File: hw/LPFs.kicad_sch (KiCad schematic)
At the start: 26 parts, among them K201 G6K-2, K202 G6K-2, K203 G6K-2, Q201 2N7002H, Q202 2N7002H, Q203 2N7002H

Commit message: Timing now closes at 121MHz. But output still does not produce any signal on my scope. Shit.
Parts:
- removed C201, C211: 100nF X7R 50V, Capacitor_SMD:C_0603_1608Metric, symbol Device:C
- L201, L204: MPN CW252016-1R2J -> 1008LS-122XJR; Mouser Part Number 1008LS-222 -> (none)
- L202, L205: MFG muRata -> (none); MPN LQW2UASR56G00L -> 1008CS-561X; Mouser Part Number 0805CS-391XGLC -> (none); Mouser_PN 81-LQW2UASR56G00L -> (none)
- L203, L206: MFG Bourns -> (none); MPN CW252016-R27J -> 1008CS-271XGRC; Mouser Part Number 0805CS-271 XGLC -> (none); Mouser_PN 652-CW252016-R27J -> 994-1008CS-271XGRC
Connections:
- net RFin: now also K201.4, K202.4, K203.4
- net RFout: now also K201.5, K202.5, K203.5

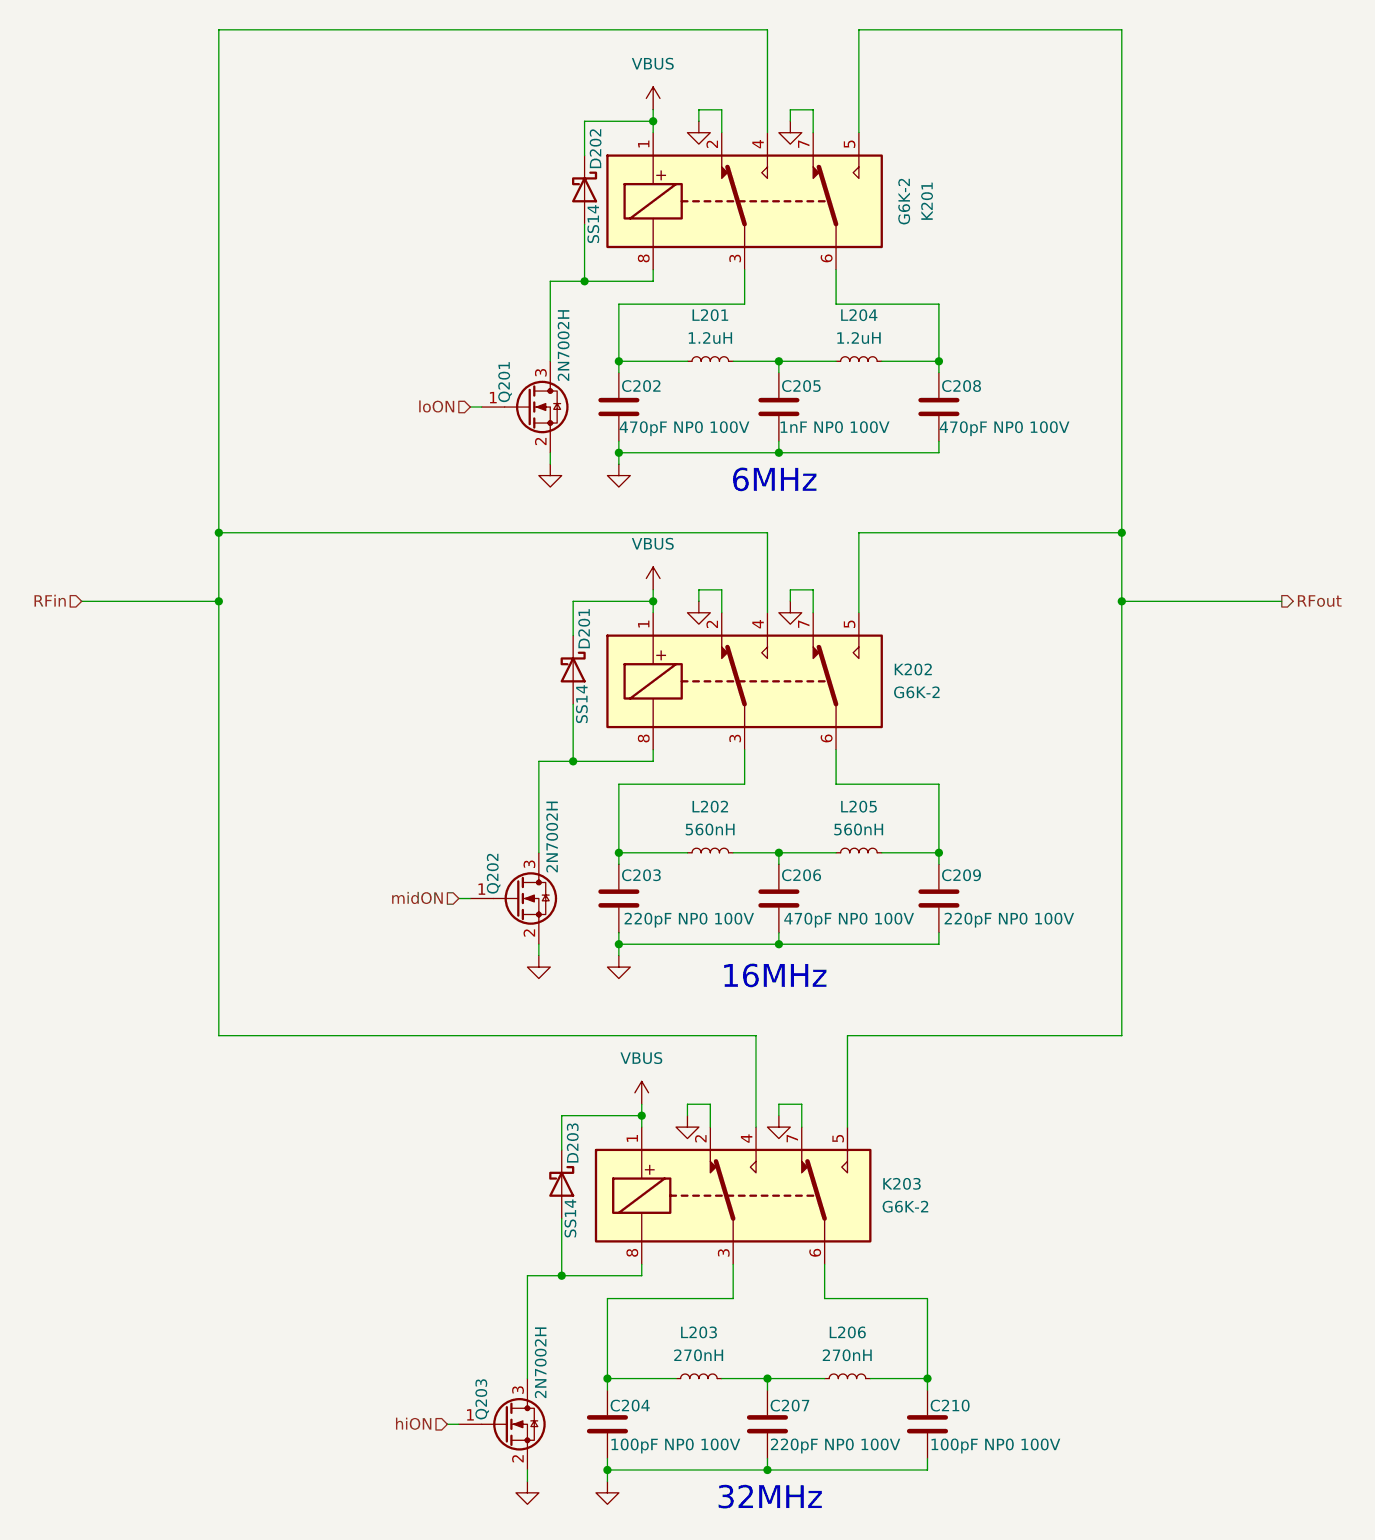
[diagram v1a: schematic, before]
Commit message: Use VFPGAIO for pullup for driverNEN. Fix some layout issues with more equal routing lengths in critical tx phase paths.
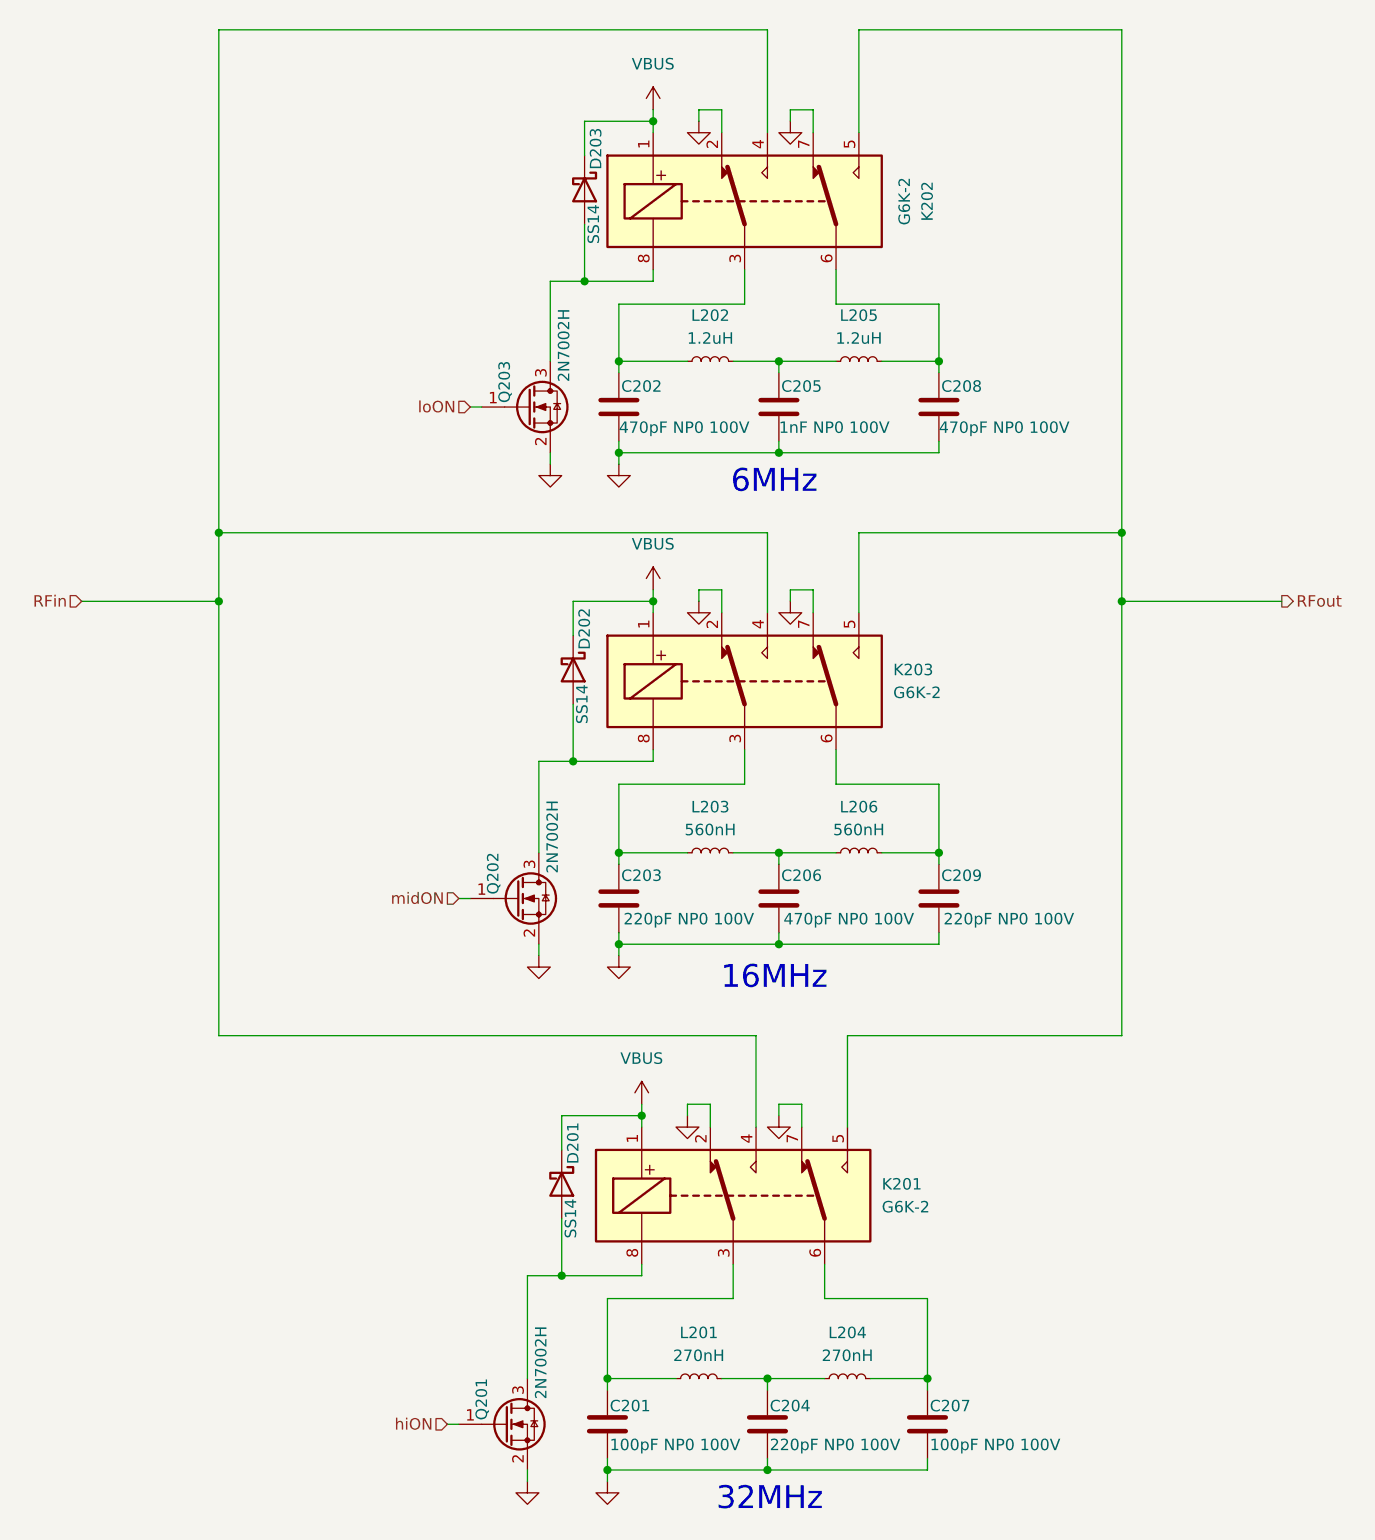
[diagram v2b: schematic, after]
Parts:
- renumbered C204 to C201, C207 to C204, C210 to C207, D203 to D201, D201 to D202, D202 to D203, K203 to K201, K201 to K202, K202 to K203, L203 to L201, L201 to L202, L202 to L203, L206 to L204, L204 to L205, L205 to L206, Q203 to Q201, Q201 to Q203

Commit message: Fucking USB 16-pin footprint! Also, completely redid the layout and wiring of the transmitter using a MOSFET gate and R+diode gate drive, simplify BOM, enhance LPFs for square wave output >= 10MHz.
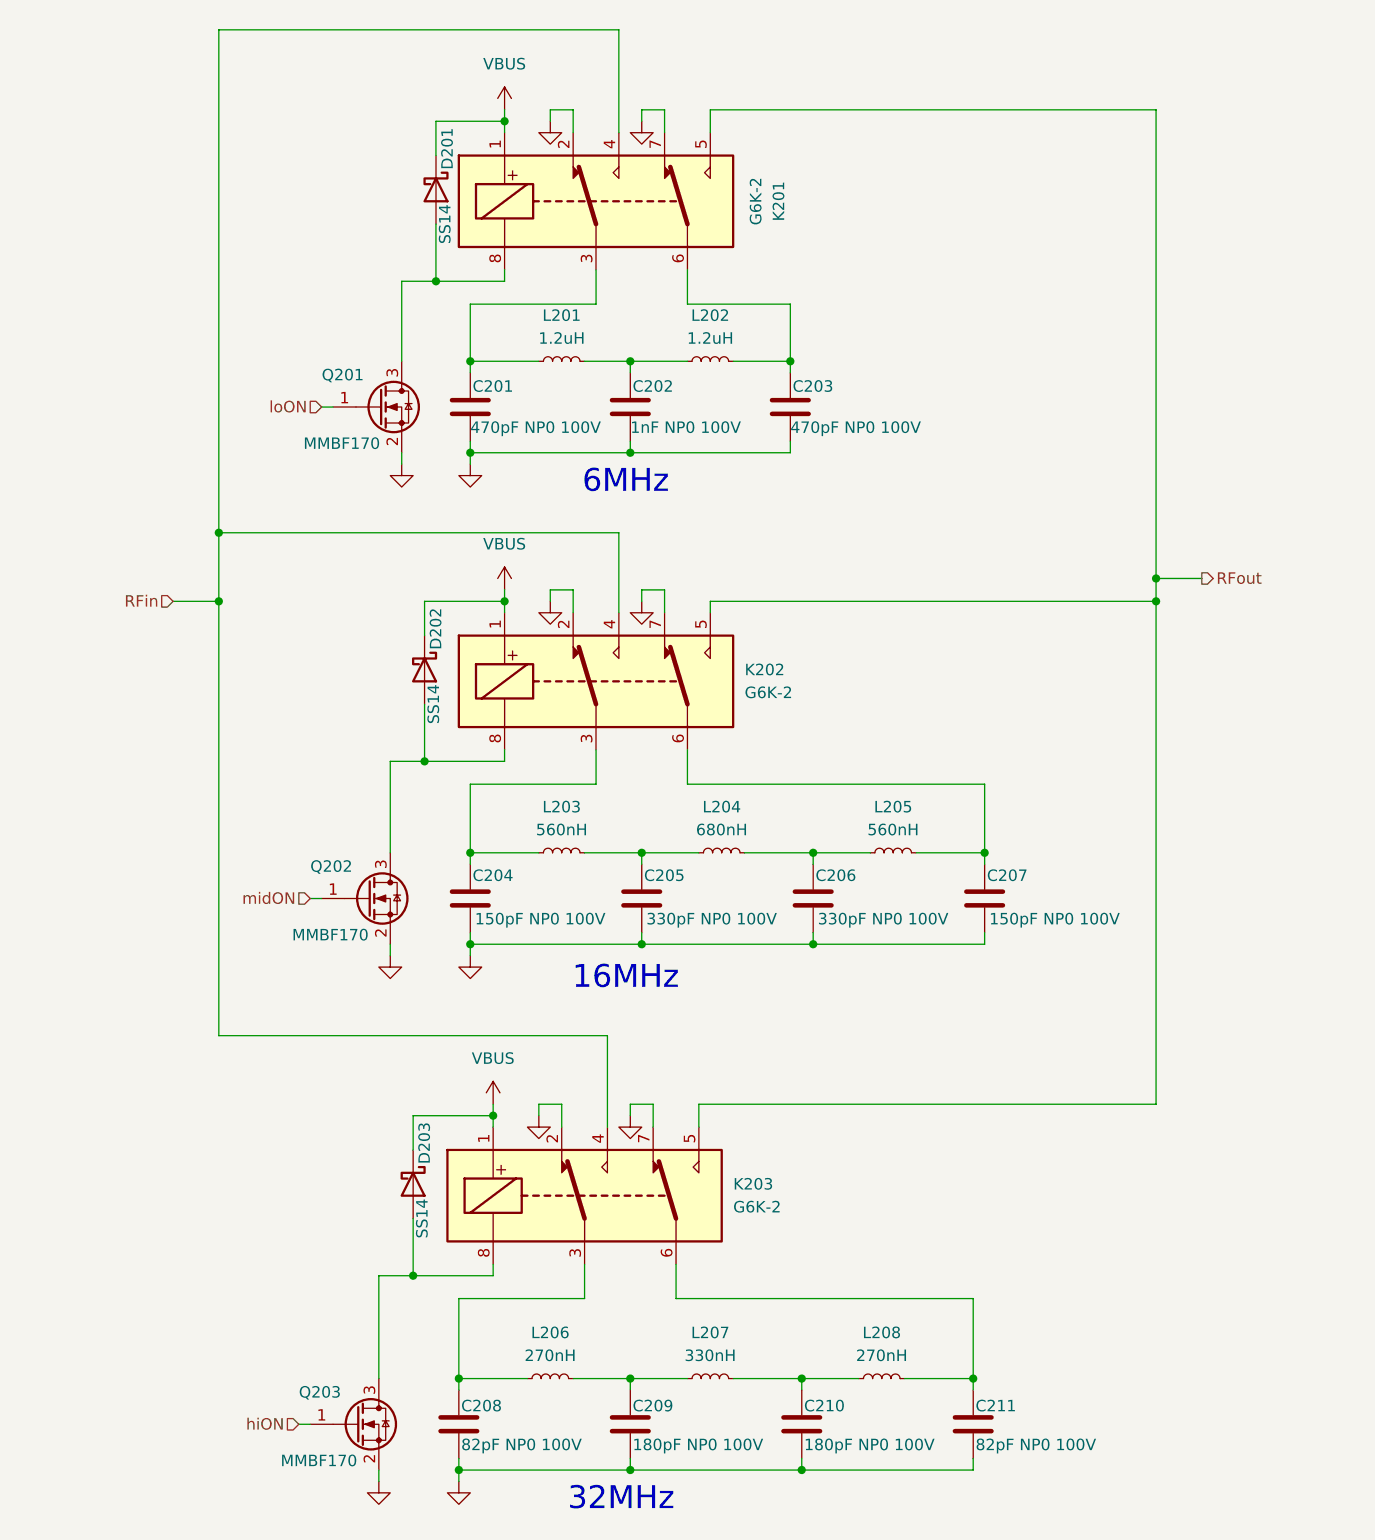
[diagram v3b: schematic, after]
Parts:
- removed Q201, Q202, Q203: 2N7002H, Package_TO_SOT_SMD:SOT-23, symbol Transistor_FET:2N7002H
- added C207: 150pF NP0 100V, Capacitor_SMD:C_0603_1608Metric, symbol Device:C
- added C211: 82pF NP0 100V, Capacitor_SMD:C_0603_1608Metric, symbol Device:C
- added L205: 560nH, Inductor_SMD:L_1008_2520Metric, symbol Device:L_Small
- added L208: 270nH, Inductor_SMD:L_0805_2012Metric, symbol Device:L_Small
- added Q201, Q202, Q203: MMBF170, Package_TO_SOT_SMD:SOT-23, symbol Transistor_FET:BS170F
- C202: renamed from C205; cap-type (none) -> X5R; working-voltage (none) -> 25V
- C204: renamed from C203; value 220pF NP0 100V -> 150pF NP0 100V; MPN GCM1885C2A221FA6D -> GRM1885C2A151JA01D; Mouser_PN 81-GCM1885C2A221FA6D -> 81-GRM1885C2A151JA01
- C205: renamed from C206; value 470pF NP0 100V -> 330pF NP0 100V; MPN GCM1885C2A471FA6D -> GRM1885C2A331JA01D; Mouser_PN 81-GCM1885C2A471FA6D -> 81-GRM185C2A331JA01D
- C206: renamed from C209; value 220pF NP0 100V -> 330pF NP0 100V; MPN GCM1885C2A221FA6D -> GRM1885C2A331JA01D; Mouser_PN 81-GCM1885C2A221FA6D -> 81-GRM185C2A331JA01D
- C208: renamed from C201; value 100pF NP0 100V -> 82pF NP0 100V
- C209: renamed from C204; value 220pF NP0 100V -> 180pF NP0 100V; MPN GCM1885C2A221FA6D -> GCM1885C2A181JA16D; Mouser_PN 81-GCM1885C2A221FA6D -> 81-GCM1885C2A181JA6D
- C210: renamed from C207; value 100pF NP0 100V -> 180pF NP0 100V; MFG Kyocera AVX -> muRata; MPN KGM15ACG2A101FT -> GCM1885C2A181JA16D; Mouser_PN 581-KGM15ACG2A101FT -> 81-GCM1885C2A181JA6D
- K201: renamed from K202; MFG (none) -> OMRON; MPN (none) -> G6K-2G-DC5; Mouser_PN (none) -> 653-G6K-2G-DC5
- K202: renamed from K203; MFG (none) -> OMRON; MPN (none) -> G6K-2G-DC5; Mouser_PN (none) -> 653-G6K-2G-DC5
- K203: renamed from K201; MFG (none) -> OMRON; MPN (none) -> G6K-2G-DC5; Mouser_PN (none) -> 653-G6K-2G-DC5
- L201: renamed from L202; MFG Bourns -> Coilcraft
- L202: renamed from L205; MFG Bourns -> Coilcraft
- L203: LCSC C6364717 -> (none); MFG (none) -> Coilcraft; MPN 1008CS-561X -> 1008CS-561XJRC; Mouser_PN (none) -> 994-1008CS-561XJRC
- L204: renamed from L206; value 560nH -> 680nH; MFG (none) -> Coilcraft; MPN 1008CS-561X -> 1008CS-681XJRC; Mouser_PN (none) -> 994-1008CS-681XJRC
- L206: renamed from L201; MFG (none) -> Coilcraft
- L207: renamed from L204; value 270nH -> 330nH; MFG (none) -> Coilcraft; MPN 1008CS-271XGRC -> 1008CS-331XGRC; Mouser_PN 994-1008CS-271XGRC -> 994-1008CS-331XGRC
- renumbered C202 to C201, C208 to C203, D203 to D201, D201 to D203
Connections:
- net GND: now also C207.2, C211.2, Q201.2 (S), Q202.2 (S), Q203.2 (S)
- net hiON: now also Q203.1 (G)
- net loON: now also Q201.1 (G)
- net midON: now also Q202.1 (G)
- net at C206.1, L204.2: now also L205.1; no longer K202.6
- net at C210.1, L207.2: now also L208.1; no longer K203.6
- net at D202.2 (A), K202.8: now also Q202.3 (D)
- net at D201.2 (A), K201.8: now also Q201.3 (D)
- net at D203.2 (A), K203.8: now also Q203.3 (D)
- new net: C207.1, K202.6, L205.2
- new net: C211.1, K203.6, L208.2
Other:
- moved on the sheet: C201, C202, C203, C204, C205, C206, C208, C209, C210, D201, D202, D203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
